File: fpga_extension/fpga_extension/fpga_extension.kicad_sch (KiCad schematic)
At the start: 0 parts

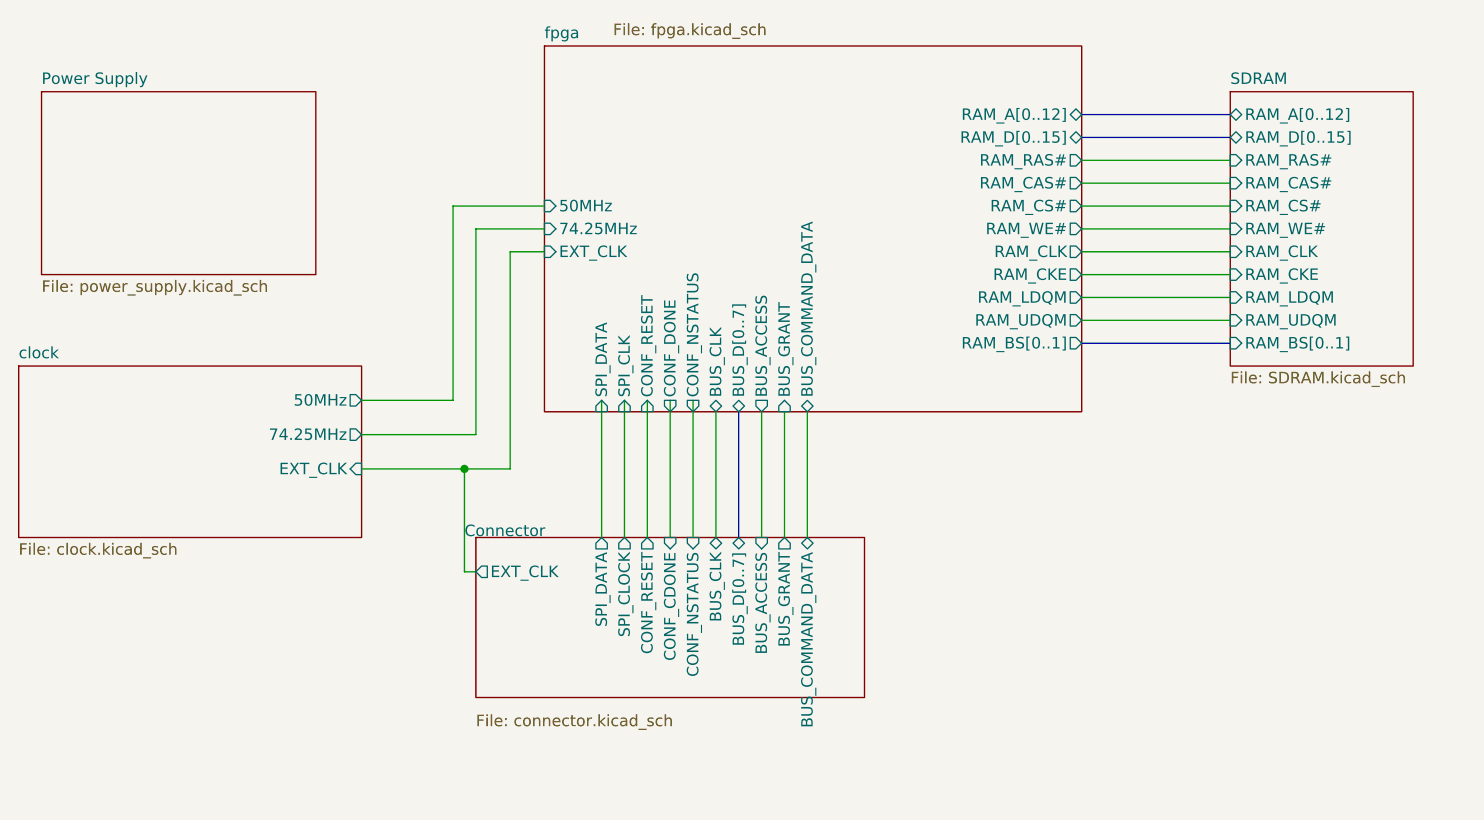
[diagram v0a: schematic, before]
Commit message: working on new version of fpga extension with Lattice FPGA
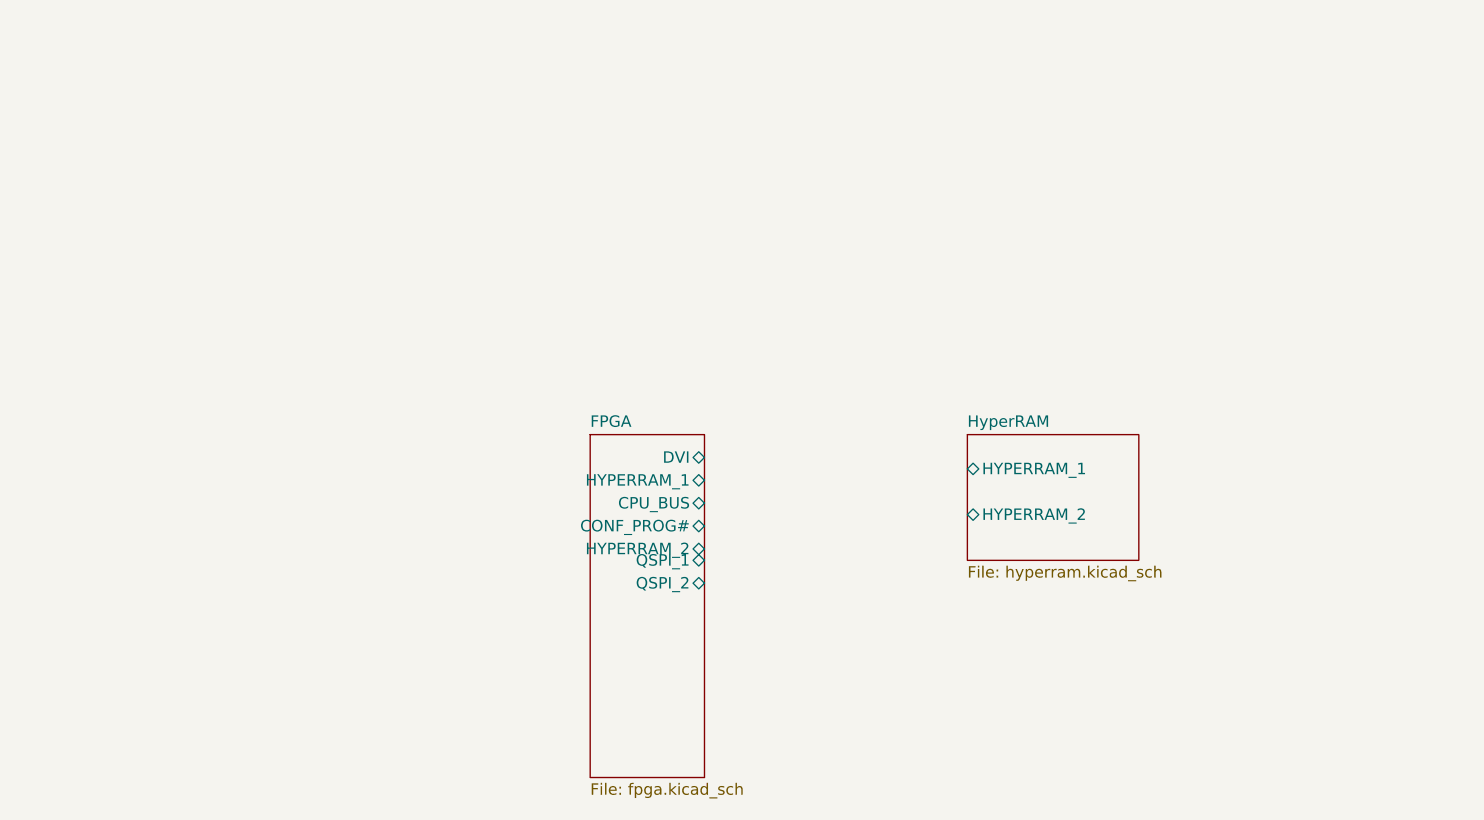
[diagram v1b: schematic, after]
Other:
- removed sheet Connector
- removed sheet Power Supply
- removed sheet SDRAM
- removed sheet clock
- removed sheet fpga
- added sheet FPGA (fpga.kicad_sch)
- added sheet HyperRAM (hyperram.kicad_sch)

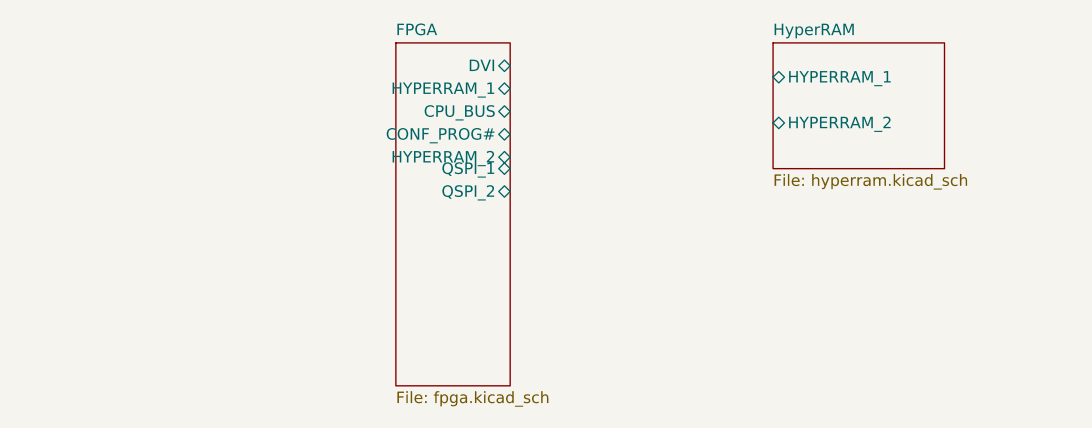
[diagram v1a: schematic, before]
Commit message: qspi added
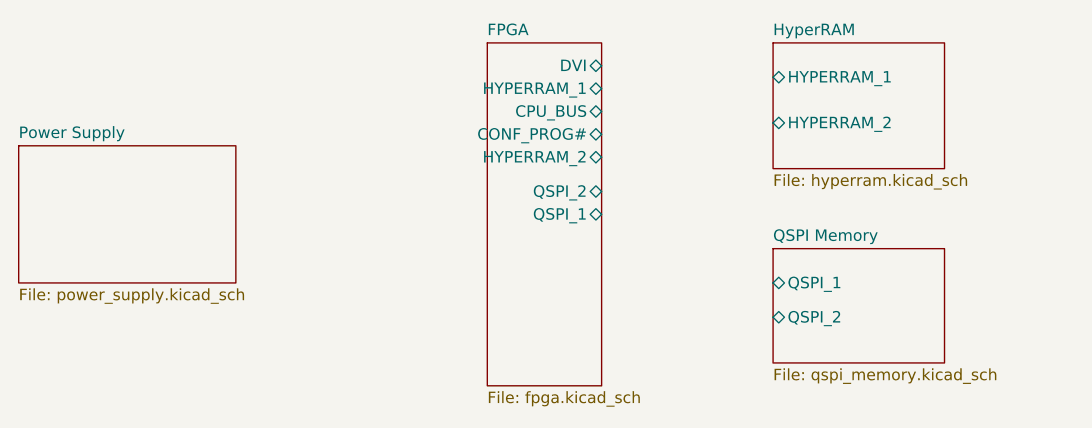
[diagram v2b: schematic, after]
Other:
- added sheet Power Supply (power_supply.kicad_sch)
- added sheet QSPI Memory (qspi_memory.kicad_sch)

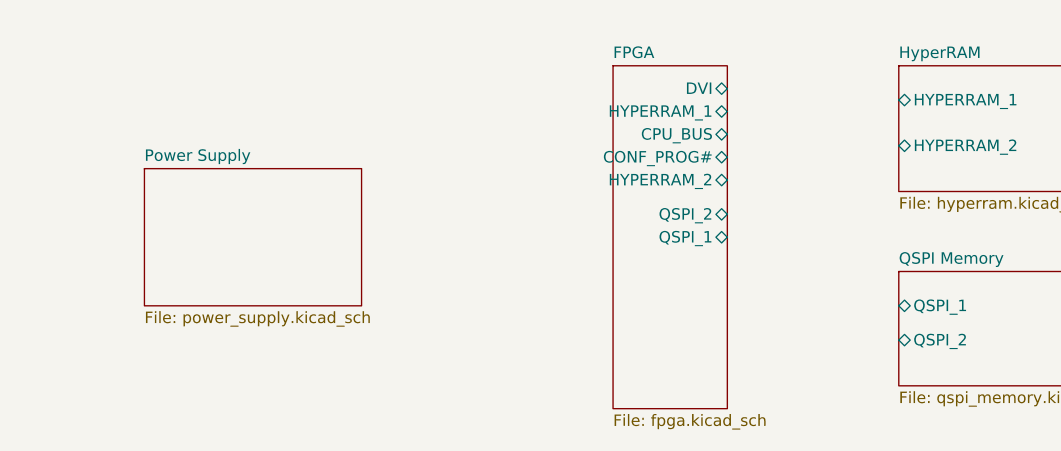
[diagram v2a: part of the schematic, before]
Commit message: some ERC fixes
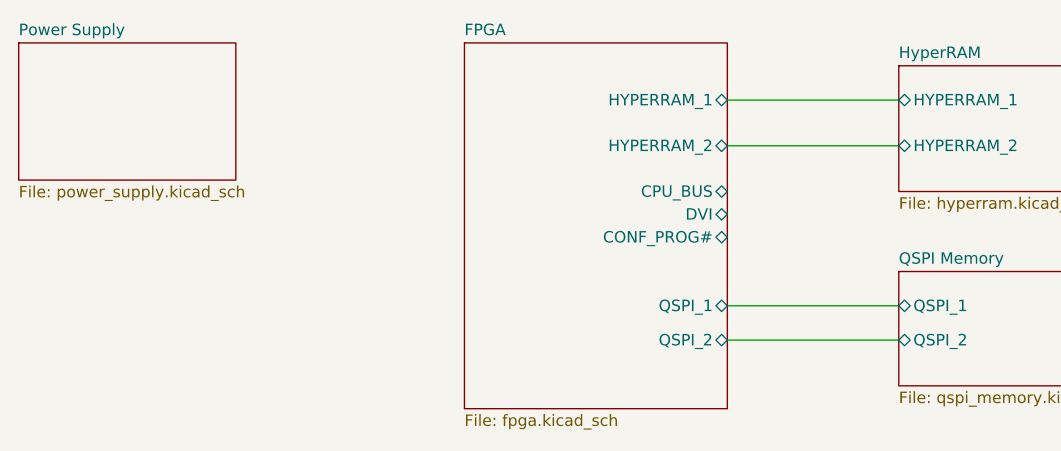
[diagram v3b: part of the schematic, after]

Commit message: refactored mainboard schematic
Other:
- removed sheet HyperRAM
- sheet FPGA ports: added none; removed DVI, HYPERRAM_1, HYPERRAM_2, QSPI_1, QSPI_2
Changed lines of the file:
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@@
     (company "Mateusz Stadnik")
-  )
-  (wire (pts (xy 137.16 88.9) (xy 156.21 88.9))
-    (stroke (width 0) (type default))
-  )
-  (wire (pts (xy 137.16 115.57) (xy 156.21 115.57))
-    (stroke (width 0) (type default))
-  )
-  (wire (pts (xy 137.16 111.76) (xy 156.21 111.76))
-    (stroke (width 0) (type default))
-  )
-  (wire (pts (xy 137.16 93.98) (xy 156.21 93.98))
-    (stroke (width 0) (type default))
   )
   (sheet (at 58.42 82.55) (size 24.13 15.24) (fields_autoplaced)
@@
       (effects (font (size 1.27 1.27)) (justify left top))
     )
-    (pin "DVI" bidirectional (at 137.16 101.6 0)
-      (effects (font (size 1.27 1.27)) (justify right))
-    )
-    (pin "HYPERRAM_1" bidirectional (at 137.16 88.9 0)
-      (effects (font (size 1.27 1.27)) (justify right))
-    )
     (pin "CPU_BUS" bidirectional (at 137.16 99.06 0)
       (effects (font (size 1.27 1.27)) (justify right))
@@
     (pin "CONF_PROG#" bidirectional (at 137.16 104.14 0)
       (effects (font (size 1.27 1.27)) (justify right))
-    )
-    (pin "HYPERRAM_2" bidirectional (at 137.16 93.98 0)
-      (effects (font (size 1.27 1.27)) (justify right))
-    )
-    (pin "QSPI_1" bidirectional (at 137.16 111.76 0)
-      (effects (font (size 1.27 1.27)) (justify right))
-    )
-    (pin "QSPI_2" bidirectional (at 137.16 115.57 0)
-      (effects (font (size 1.27 1.27)) (justify right))
-    )
-  )
-  (sheet (at 156.21 85.09) (size 19.05 13.97) (fields_autoplaced)
-    (stroke (width 0.1524) (type solid))
-    (fill (color 0 0 0 0.0000))
-    (property "Sheetname" "HyperRAM" (at 156.21 84.3784 0)
-      (effects (font (size 1.27 1.27)) (justify left bottom))
-    )
-    (property "Sheetfile" "hyperram.kicad_sch" (at 156.21 99.6446 0)
-      (effects (font (size 1.27 1.27)) (justify left top))
-    )
-    (pin "HYPERRAM_1" bidirectional (at 156.21 88.9 180)
-      (effects (font (size 1.27 1.27)) (justify left))
-    )
-    (pin "HYPERRAM_2" bidirectional (at 156.21 93.98 180)
-      (effects (font (size 1.27 1.27)) (justify left))
     )
   )
@@
     (path "/a6f73e0d-9cce-49ab-8363-cdcc30f9e355/138c08cd-f315-49a6-890d-a48ba5f28fe6/1dde2c5a-9472-4da9-baa6-1a560aaf54f6" (page "5"))
     (path "/a6f73e0d-9cce-49ab-8363-cdcc30f9e355/138c08cd-f315-49a6-890d-a48ba5f28fe6/163e4125-8e51-44a8-bfe7-73013b4370b0" (page "6"))
-    (path "/a6f73e0d-9cce-49ab-8363-cdcc30f9e355/191072c1-f1a0-4628-a85c-1b220f5a8dbe" (page "7"))
-    (path "/a6f73e0d-9cce-49ab-8363-cdcc30f9e355/138c08cd-f315-49a6-890d-a48ba5f28fe6/9c404515-8db6-4333-9ae5-8b98f2cc5e89" (page "8"))
     (path "/a6f73e0d-9cce-49ab-8363-cdcc30f9e355/138c08cd-f315-49a6-890d-a48ba5f28fe6/0b1b5c70-1f64-4928-ac3a-4f98af1b6ecc" (page "9"))
     (path "/a6f73e0d-9cce-49ab-8363-cdcc30f9e355/50a7b31e-7ebf-40b9-aea8-607bd559467f" (page "10"))

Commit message: prepared first versions of PCBs
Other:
- removed sheet FPGA
- removed sheet Power Supply
- removed sheet QSPI Memory
- added sheet Connector (connector.kicad_sch)
- added sheet FPGA Configuration (fpga_config.kicad_sch)
- added sheet JTAG (jtag_programmer.kicad_sch)
- added sheet LEDs (leds.kicad_sch)
- added sheet MSPC BUS (mspc_bus.kicad_sch)
- added sheet Power (power.kicad_sch)
- added sheet RAM (ram.kicad_sch)
- added sheet SD (card_slot.kicad_sch)
- added sheet Unused Banks (unused_banks.kicad_sch)
- company: Mateusz Stadnik -> (none)
- title: FPGA schematic -> (none)
